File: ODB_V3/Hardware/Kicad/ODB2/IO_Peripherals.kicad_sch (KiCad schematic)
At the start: 33 parts, among them J1 142-0701-801, J2 Conn_02x04_Odd_Even, J3 IdeFIX_GT17HN-4DP-2HA56, J4 MEM2067, J5 RFD_GT17HN-4DP-2HA56, J7 SYS_SW_Conn_01x05_Header, J8 USB_B_Micro, J9 USBLC6-2P6, Q1 MMBT3904, U15 W25Q512JVEIQ, U3 HM11, U5 L76L-M33

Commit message: wip: fix not connected VDD + traces
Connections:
- net +3V3: now also J4.4 (VDD)

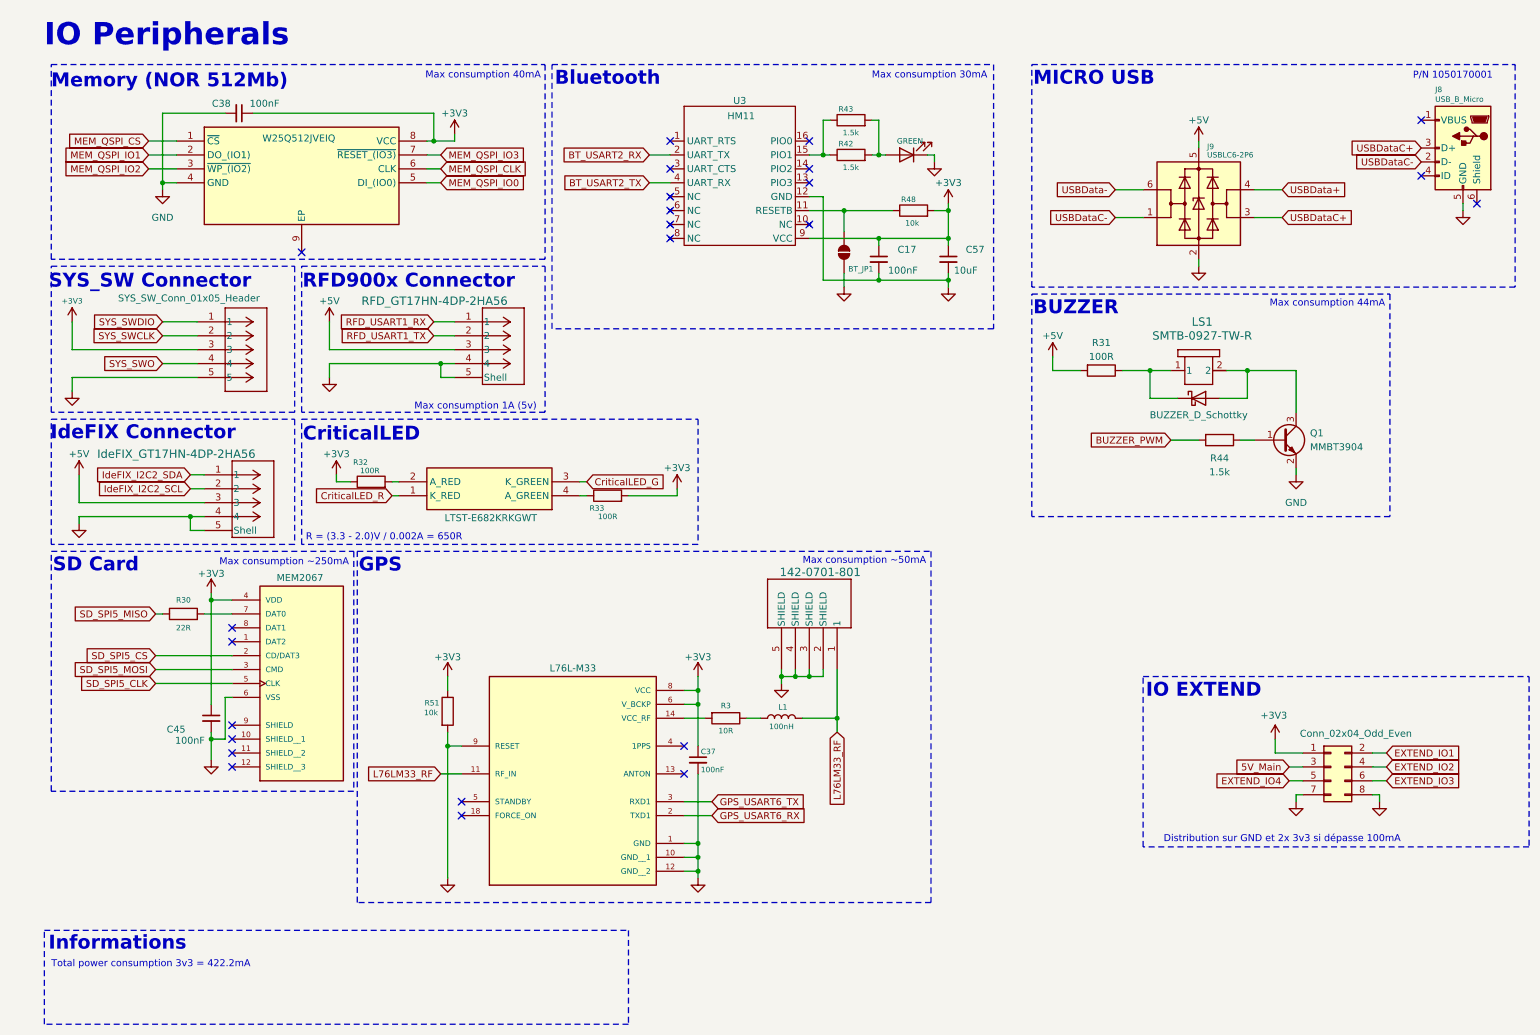
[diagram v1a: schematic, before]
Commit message: wip : début refdes sur silkscreen
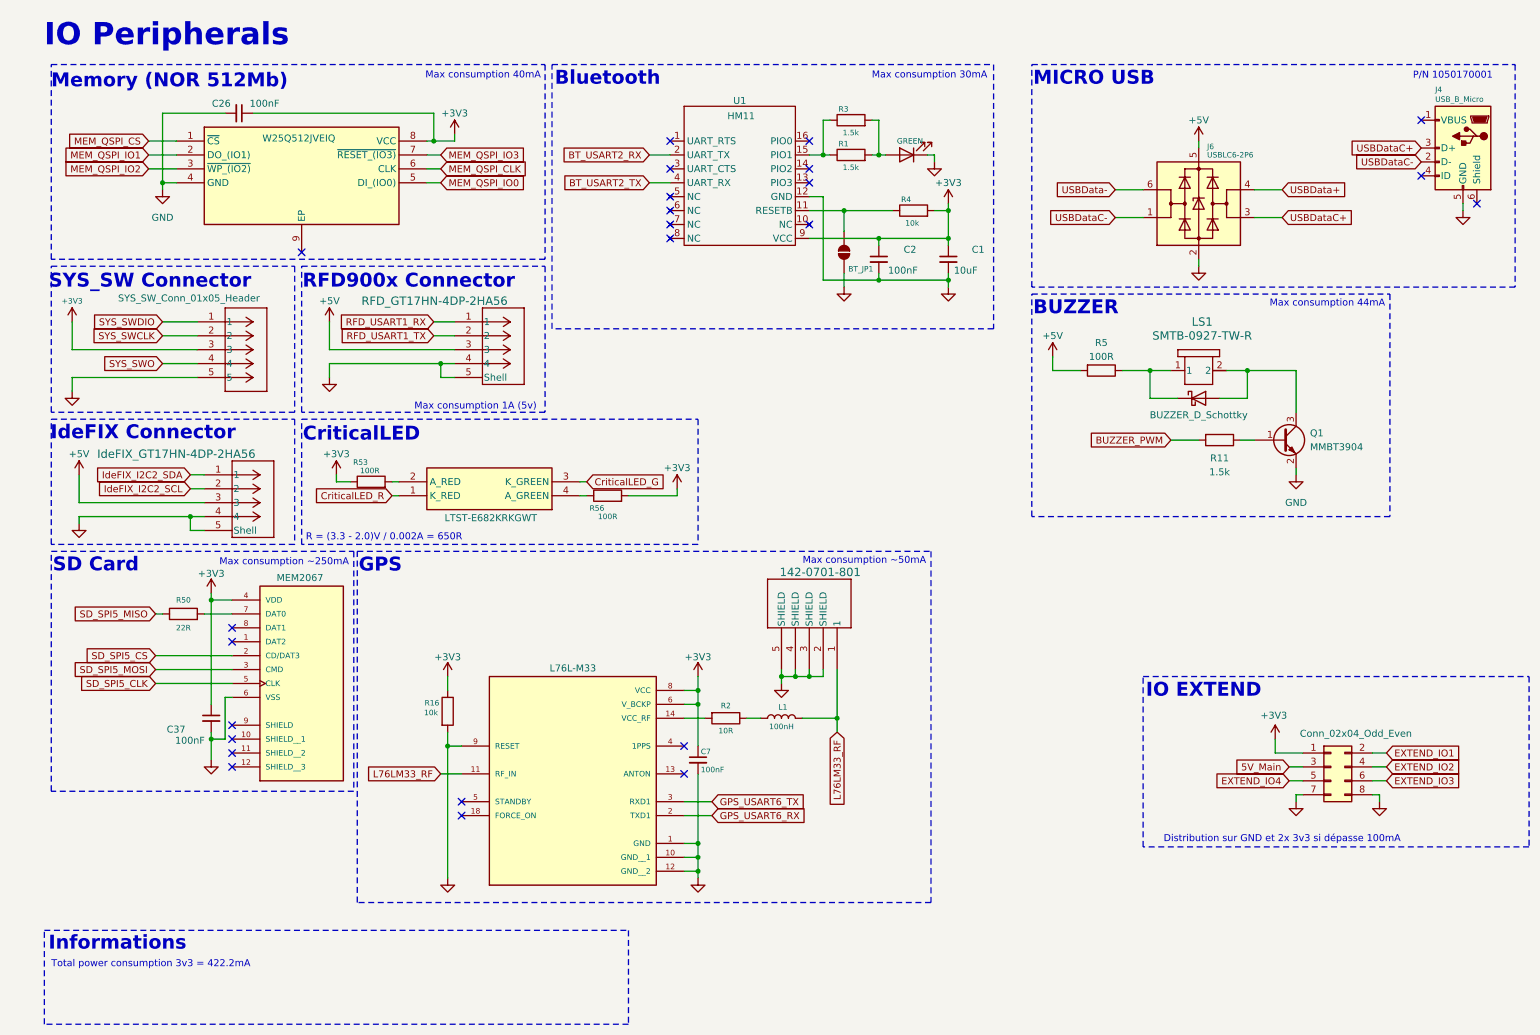
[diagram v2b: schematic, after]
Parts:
- renumbered C57 to C1, C17 to C2, C38 to C26, C45 to C37, C37 to C7, D12 to D1, D9 to D2, D13 to D6, J4 to J10, J3 to J2, J5 to J3, J8 to J4, J7 to J5, J9 to J6, J2 to J7, R42 to R1, R44 to R11, R51 to R16, R3 to R2, R43 to R3, R48 to R4, R31 to R5, R30 to R50, R32 to R53, R33 to R56, U3 to U1, U5 to U2, U15 to U9
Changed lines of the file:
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@@
 		(on_board yes)
 		(dnp no)
-		(property "Reference" "R33"
+		(property "Reference" "R56"
 			(at 112.268 102.616 90)
 			(effects
@@
 			(project "ODB2"
 				(path "/4b06c5d1-aa8b-48ed-8972-b43a60cfab78/93865dc8-71fa-4dc6-90ce-f5a9779dfd41"
-					(reference "R33")
+					(reference "R56")
 					(unit 1)
 				)
@@
 		(on_board yes)
 		(dnp no)
-		(property "Reference" "U15"
+		(property "Reference" "U9"
 			(at 78.74 27.94 0)
 			(effects
@@
 			(project ""
 				(path "/4b06c5d1-aa8b-48ed-8972-b43a60cfab78/93865dc8-71fa-4dc6-90ce-f5a9779dfd41"
-					(reference "U15")
+					(reference "U9")
 					(unit 1)
 				)
@@
 		(on_board yes)
 		(dnp no)
-		(property "Reference" "R48"
+		(property "Reference" "R4"
 			(at 169.164 46.228 90)
 			(effects
@@
 			(project "ODB2"
 				(path "/4b06c5d1-aa8b-48ed-8972-b43a60cfab78/93865dc8-71fa-4dc6-90ce-f5a9779dfd41"
-					(reference "R48")
+					(reference "R4")
 					(unit 1)
 				)
@@
 		(on_board yes)
 		(dnp no)
-		(property "Reference" "J4"
+		(property "Reference" "J10"
 			(at 52.07 116.8283 0)
 			(effects
@@
 			(project ""
 				(path "/4b06c5d1-aa8b-48ed-8972-b43a60cfab78/93865dc8-71fa-4dc6-90ce-f5a9779dfd41"
-					(reference "J4")
+					(reference "J10")
 					(unit 1)
 				)
@@
 		(on_board yes)
 		(dnp no)
-		(property "Reference" "J5"
+		(property "Reference" "J3"
 			(at 101.6 71.1199 0)
 			(effects
@@
 			(project ""
 				(path "/4b06c5d1-aa8b-48ed-8972-b43a60cfab78/93865dc8-71fa-4dc6-90ce-f5a9779dfd41"
-					(reference "J5")
+					(reference "J3")
 					(unit 1)
 				)
@@
 		(on_board yes)
 		(dnp no)
-		(property "Reference" "C45"
+		(property "Reference" "C37"
 			(at 35.052 143.002 0)
 			(effects
@@
 			(project "ODB2"
 				(path "/4b06c5d1-aa8b-48ed-8972-b43a60cfab78/93865dc8-71fa-4dc6-90ce-f5a9779dfd41"
-					(reference "C45")
+					(reference "C37")
 					(unit 1)
 				)
@@
 		(on_board yes)
 		(dnp no)
-		(property "Reference" "R42"
+		(property "Reference" "R1"
 			(at 157.734 36.068 90)
 			(effects
@@
 			(project "ODB2"
 				(path "/4b06c5d1-aa8b-48ed-8972-b43a60cfab78/93865dc8-71fa-4dc6-90ce-f5a9779dfd41"
-					(reference "R42")
+					(reference "R1")
 					(unit 1)
 				)
@@
 		(on_board yes)
 		(dnp no)
-		(property "Reference" "R31"
+		(property "Reference" "R5"
 			(at 205.74 72.39 90)
 			(effects
@@
 			(project ""
 				(path "/4b06c5d1-aa8b-48ed-8972-b43a60cfab78/93865dc8-71fa-4dc6-90ce-f5a9779dfd41"
-					(reference "R31")
+					(reference "R5")
 					(unit 1)
 				)
@@
 		(on_board yes)
 		(dnp no)
-		(property "Reference" "C38"
+		(property "Reference" "C26"
 			(at 46.736 28.702 90)
 			(effects
@@
 			(project "ODB2"
 				(path "/4b06c5d1-aa8b-48ed-8972-b43a60cfab78/93865dc8-71fa-4dc6-90ce-f5a9779dfd41"
-					(reference "C38")
+					(reference "C26")
 					(unit 1)
 				)
@@
 		(on_board yes)
 		(dnp no)
-		(property "Reference" "U3"
+		(property "Reference" "U1"
 			(at 139.7 28.194 0)
 			(effects
@@
 			(project ""
 				(path "/4b06c5d1-aa8b-48ed-8972-b43a60cfab78/93865dc8-71fa-4dc6-90ce-f5a9779dfd41"
-					(reference "U3")
+					(reference "U1")
 					(unit 1)
 				)
@@
 		(on_board yes)
 		(dnp no)
-		(property "Reference" "R30"
+		(property "Reference" "R50"
 			(at 38.1 119.38 90)
 			(effects
@@
 			(project "ODB2"
 				(path "/4b06c5d1-aa8b-48ed-8972-b43a60cfab78/93865dc8-71fa-4dc6-90ce-f5a9779dfd41"
-					(reference "R30")
+					(reference "R50")
 					(unit 1)
 				)
@@
 		(on_board yes)
 		(dnp no)
-		(property "Reference" "J9"
+		(property "Reference" "J6"
 			(at 225.044 36.576 0)
 			(effects
@@
 			(project "ODB2"
 				(path "/4b06c5d1-aa8b-48ed-8972-b43a60cfab78/93865dc8-71fa-4dc6-90ce-f5a9779dfd41"
-					(reference "J9")
+					(reference "J6")
 					(unit 1)
 				)
@@
 		(on_board yes)
 		(dnp no)
-		(property "Reference" "R51"
+		(property "Reference" "R16"
 			(at 84.836 138.176 0)
 			(effects
@@
 			(project "ODB2"
 				(path "/4b06c5d1-aa8b-48ed-8972-b43a60cfab78/93865dc8-71fa-4dc6-90ce-f5a9779dfd41"
-					(reference "R51")
+					(reference "R16")
 					(unit 1)
 				)
@@
 		(on_board yes)
 		(dnp no)
-		(property "Reference" "R3"
+		(property "Reference" "R2"
 			(at 137.16 138.684 90)
 			(effects
@@
 			(project "ODB2"
 				(path "/4b06c5d1-aa8b-48ed-8972-b43a60cfab78/93865dc8-71fa-4dc6-90ce-f5a9779dfd41"
-					(reference "R3")
+					(reference "R2")
 					(unit 1)
 				)
@@
 		(on_board yes)
 		(dnp no)
-		(property "Reference" "J8"
+		(property "Reference" "J4"
 			(at 266.7 26.162 0)
 			(effects
@@
 			(project "ODB2"
 				(path "/4b06c5d1-aa8b-48ed-8972-b43a60cfab78/93865dc8-71fa-4dc6-90ce-f5a9779dfd41"
-					(reference "J8")
+					(reference "J4")
 					(unit 1)
 				)
@@
 		(on_board yes)
 		(dnp no)
-		(property "Reference" "J7"
+		(property "Reference" "J5"
 			(at 43.434 61.468 0)
 			(effects
@@
 			(project ""
 				(path "/4b06c5d1-aa8b-48ed-8972-b43a60cfab78/93865dc8-71fa-4dc6-90ce-f5a9779dfd41"
-					(reference "J7")
+					(reference "J5")
 					(unit 1)
 				)
@@
 		(on_board yes)
 		(dnp no)
-		(property "Reference" "U5"
+		(property "Reference" "U2"
 			(at 93.98 132.588 0)
 			(effects
@@
 			(project ""
 				(path "/4b06c5d1-aa8b-48ed-8972-b43a60cfab78/93865dc8-71fa-4dc6-90ce-f5a9779dfd41"
-					(reference "U5")
+					(reference "U2")
 					(unit 1)
 				)
@@
 		(on_board yes)
 		(dnp no)
-		(property "Reference" "D12"
+		(property "Reference" "D1"
 			(at 166.624 35.56 0)
 			(effects
@@
 			(project "ODB2"
 				(path "/4b06c5d1-aa8b-48ed-8972-b43a60cfab78/93865dc8-71fa-4dc6-90ce-f5a9779dfd41"
-					(reference "D12")
+					(reference "D1")
 					(unit 1)
 				)
@@
 		(on_board yes)
 		(dnp no)
-		(property "Reference" "R43"
+		(property "Reference" "R3"
 			(at 157.734 29.718 90)
 			(effects
@@
 			(project "ODB2"
 				(path "/4b06c5d1-aa8b-48ed-8972-b43a60cfab78/93865dc8-71fa-4dc6-90ce-f5a9779dfd41"
-					(reference "R43")
+					(reference "R3")
 					(unit 1)
 				)
@@
 		(on_board yes)
 		(dnp no)
-		(property "Reference" "R44"
+		(property "Reference" "R11"
 			(at 227.33 93.472 90)
 			(effects
@@
 			(project ""
 				(path "/4b06c5d1-aa8b-48ed-8972-b43a60cfab78/93865dc8-71fa-4dc6-90ce-f5a9779dfd41"
-					(reference "R44")
+					(reference "R11")
 					(unit 1)
 				)
@@
 		(on_board yes)
 		(dnp no)
-		(property "Reference" "C17"
+		(property "Reference" "C2"
 			(at 171.958 55.372 0)
 			(effects
@@
 			(project "ODB2"
 				(path "/4b06c5d1-aa8b-48ed-8972-b43a60cfab78/93865dc8-71fa-4dc6-90ce-f5a9779dfd41"
-					(reference "C17")
+					(reference "C2")
 					(unit 1)
 				)
@@
 		(on_board yes)
 		(dnp no)
-		(property "Reference" "C57"
+		(property "Reference" "C1"
 			(at 184.404 55.372 0)
 			(effects
@@
 			(project "ODB2"
 				(path "/4b06c5d1-aa8b-48ed-8972-b43a60cfab78/93865dc8-71fa-4dc6-90ce-f5a9779dfd41"
-					(reference "C57")
+					(reference "C1")
 					(unit 1)
 				)
@@
 		(on_board yes)
 		(dnp no)
-		(property "Reference" "R32"
+		(property "Reference" "R53"
 			(at 69.088 94.234 90)
 			(effects
@@
 			(project "ODB2"
 				(path "/4b06c5d1-aa8b-48ed-8972-b43a60cfab78/93865dc8-71fa-4dc6-90ce-f5a9779dfd41"
-					(reference "R32")
+					(reference "R53")
 					(unit 1)
 				)
@@
 		(on_board yes)
 		(dnp no)
-		(property "Reference" "D13"
+		(property "Reference" "D6"
 			(at 96.774 107.188 0)
 			(effects
@@
 			(project "ODB2"
 				(path "/4b06c5d1-aa8b-48ed-8972-b43a60cfab78/93865dc8-71fa-4dc6-90ce-f5a9779dfd41"
-					(reference "D13")
+					(reference "D6")
 					(unit 1)
 				)
@@
 		(on_board yes)
 		(dnp no)
-		(property "Reference" "C37"
+		(property "Reference" "C7"
 			(at 132.588 147.066 0)
 			(effects
@@
 			(project "ODB2"
 				(path "/4b06c5d1-aa8b-48ed-8972-b43a60cfab78/93865dc8-71fa-4dc6-90ce-f5a9779dfd41"
-					(reference "C37")
+					(reference "C7")
 					(unit 1)
 				)
@@
 		(on_board yes)
 		(dnp no)
-		(property "Reference" "J3"
+		(property "Reference" "J2"
 			(at 55.88 99.0599 0)
 			(effects
@@
 			(project "ODB2"
 				(path "/4b06c5d1-aa8b-48ed-8972-b43a60cfab78/93865dc8-71fa-4dc6-90ce-f5a9779dfd41"
-					(reference "J3")
+					(reference "J2")
 					(unit 1)
 				)
@@
 		(on_board yes)
 		(dnp no)
-		(property "Reference" "J2"
+		(property "Reference" "J7"
 			(at 248.92 140.97 0)
 			(effects
@@
 			(project ""
 				(path "/4b06c5d1-aa8b-48ed-8972-b43a60cfab78/93865dc8-71fa-4dc6-90ce-f5a9779dfd41"
-					(reference "J2")
+					(reference "J7")
 					(unit 1)
 				)
@@
 		(on_board yes)
 		(dnp no)
-		(property "Reference" "D9"
+		(property "Reference" "D2"
 			(at 223.2025 76.2 0)
 			(effects
@@
 			(project ""
 				(path "/4b06c5d1-aa8b-48ed-8972-b43a60cfab78/93865dc8-71fa-4dc6-90ce-f5a9779dfd41"
-					(reference "D9")
+					(reference "D2")
 					(unit 1)
 				)
